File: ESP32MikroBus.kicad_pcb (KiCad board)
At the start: 4 copper layers, 30.2 x 44.5 mm, 27 parts, among them IC1 ESP32-C6-WROOM-1-N4, IC2 AP7361C-33ER-13, J1 USB4105GFA120, J2 CON_HDR_MIKROBUS_SOCKET_TH, J3 Qwiic, U1 USBLC6-2P6

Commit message: PCB Layout v1.0 ready for verification by PCBWay
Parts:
- added G***: OpenSourceHardware_Logo, tecnova:OpenSourceHardware_Logo, B.Cu at (35.8, 43.3)
- added G***: LOGO, tecnova:Tecnova_logo, B.Cu at (54.7, 42.8)
- added G***: MikroBus_Logo, tecnova:MikroBus_Logo, B.Cu at (43.8, 63.2)
- added J4: Conn_01x06, Connector_PinHeader_1.27mm:PinHeader_1x06_P1.27mm_Vertical, F.Cu at (57.2, 47.4)
- moved R4 15.1 mm to (51.2, 68.7)
- moved R2 14.8 mm to (51.2, 71.8), turned to -90 degrees
- moved TP1 12.7 mm to (50.5, 46.2)
- moved FID2 9.62 mm to (58.5, 39.0)
- moved FID3 8.83 mm to (36.6, 60.4)
- moved FID1 6.46 mm to (30.1, 80.8)
- moved C5 4.89 mm to (50.0, 64.6), turned to 90 degrees
- moved R5 4.80 mm to (41.0, 70.1)
- moved U1 3.65 mm to (43.5, 70.0), turned to 90 degrees
- moved C4 3.32 mm to (50.0, 60.5), turned to -90 degrees
- moved R6 2.21 mm to (46.0, 70.0)
- moved F1 1.75 mm to (48.2, 69.2), turned to -90 degrees
- moved R3 1.00 mm to (56.2, 56.7)
- moved R8 0.53 mm to (56.5, 44.2)
- moved J2 0.12 mm to (44.2, 69.3)
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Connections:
- C5 pad 1: Net-(IC2-IN) -> +5V
- F1 pad 1: +VBUS -> +5V
- F1 pad 2: +5V -> +VBUS
- IC1 pad 10: unconnected-(IC1-IO8-Pad10) -> /MB_MISO
- IC1 pad 11: unconnected-(IC1-IO10-Pad11) -> /MB_SCK
- IC1 pad 12: unconnected-(IC1-IO11-Pad12) -> /MB_CS
- IC1 pad 16: unconnected-(IC1-IO18-Pad16) -> /SPARE6
- IC1 pad 17: unconnected-(IC1-IO19-Pad17) -> /SPARE5
- IC1 pad 18: unconnected-(IC1-IO20-Pad18) -> /SPARE4
- IC1 pad 19: unconnected-(IC1-IO21-Pad19) -> /SPARE3
- IC1 pad 20: unconnected-(IC1-IO22-Pad20) -> /SPARE2
- IC1 pad 21: unconnected-(IC1-IO23-Pad21) -> /SPARE1
- IC1 pad 26: unconnected-(IC1-IO3-Pad26) -> /MB_PWM
- IC1 pad 27: unconnected-(IC1-IO2-Pad27) -> /USR_LED
- IC1 pad 4: unconnected-(IC1-IO4-Pad4) -> /MB_INT
- IC1 pad 5: unconnected-(IC1-IO5-Pad5) -> /MB_RST
- IC1 pad 9: unconnected-(IC1-IO1-Pad9) -> /MB_MOSI
- IC2 pad 3: Net-(IC2-IN) -> +5V
- J2 pad 15: Net-(J2-+5V) -> +5V
- R3 pad 1: +3V3 -> +3.3V
- R7 pad 1: Net-(R7-Pad1) -> +5V
- S1 pad 4: Net-(S1-Pad4) -> GND
- S1 pad 6: Net-(S1-Pad4) -> GND
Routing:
- net GND: track 0.00 -> 78.3 mm, vias 0 -> 12
- net +3.3V: track 0.00 -> 61.1 mm, vias 0 -> 9
- net /I2C_SDA: track 0.00 -> 55.7 mm, vias 0 -> 2
- net /I2C_SCL: track 0.00 -> 47.9 mm, vias 0 -> 2
- net /TXD: track 0.00 -> 35.6 mm
- net /RXD: track 0.00 -> 32.3 mm
- net /MB_INT: track 0.00 -> 31.5 mm, vias 0 -> 1
- net /MB_MOSI: track 0.00 -> 29.1 mm
- net /MB_RST: track 0.00 -> 27.4 mm, vias 0 -> 1
- net /MB_PWM: track 0.00 -> 26.2 mm, vias 0 -> 1
- net /MB_MISO: track 0.00 -> 25.1 mm
- net /MB_SCK: track 0.00 -> 21.2 mm
- net +5V: track 0.00 -> 19.4 mm
- net /USB_D_MIN: track 0.00 -> 18.7 mm, vias 0 -> 2
- net /USB_D_PLUS: track 0.00 -> 18.7 mm, vias 0 -> 2
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- added copper zone on In2.Cu, net +3.3V
- added copper zone on In2.Cu, net +VBUS
- added copper zone on In1.Cu, net GND
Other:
- board size 30.2 x 44.5 mm -> 31 x 44.8 mm
- board text added: "ESP32C6 + mikroBUS v1.0"
- board text added: "Reset"

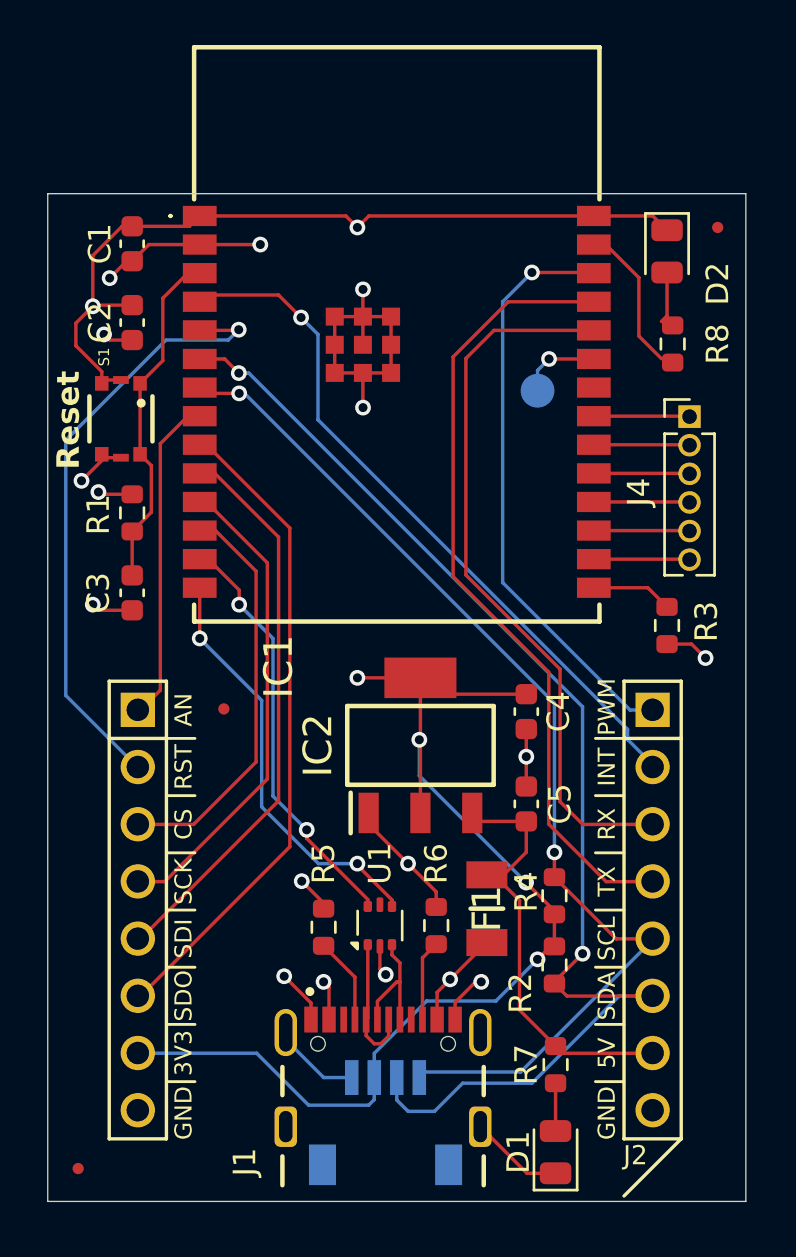
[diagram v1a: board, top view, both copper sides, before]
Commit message: Minor update, mainly cosmetical + vbus not connected
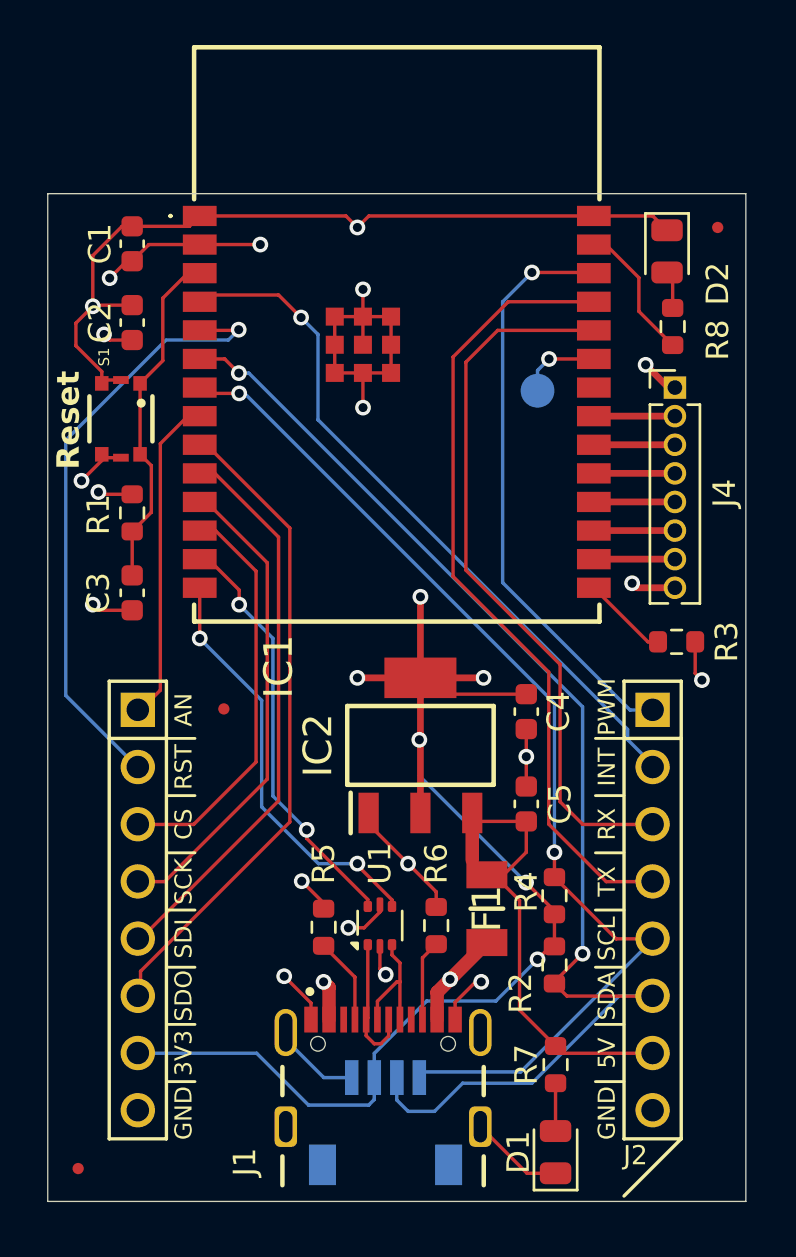
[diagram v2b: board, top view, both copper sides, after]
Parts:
- J4: value Conn_01x06 -> Conn_01x08; footprint Connector_PinHeader_1.27mm:PinHeader_1x06_P1.27mm_Vertical -> Connector_PinHeader_1.27mm:PinHeader_1x08_P1.27mm_Vertical
- moved J4 1.44 mm to (56.6, 46.1)
- moved R3 0.84 mm to (56.7, 57.4), turned to 180 degrees
- moved R8 0.77 mm to (56.5, 43.4)
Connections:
- J4 pad 1: /SPARE1 -> +3.3V
- J4 pad 2: /SPARE2 -> /SPARE1
- J4 pad 3: /SPARE3 -> /SPARE2
- J4 pad 4: /SPARE4 -> /SPARE3
- J4 pad 5: /SPARE5 -> /SPARE4
- J4 pad 6: /SPARE6 -> /SPARE5
- U1 pad 5: Net-(U1-VBUS) -> +VBUS
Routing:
- net +3.3V: track 61.1 -> 69.1 mm, vias 9 -> 12
- net +5V: track 19.4 -> 22.4 mm
- net +VBUS: track 6.11 -> 8.12 mm, vias 2 -> 3
- net GND: track 78.3 -> 80.2 mm, vias 12 -> 13
- net /SPARE6: track 4.26 -> 3.60 mm
- net /SPARE4: track 4.26 -> 3.60 mm
- net /SPARE2: track 4.26 -> 3.60 mm
- net /SPARE5: track 4.26 -> 3.60 mm
- net /SPARE3: track 4.26 -> 3.60 mm
- net /SPARE1: track 4.26 -> 3.63 mm
- net Net-(D2-A): track 2.28 -> 1.68 mm

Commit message: Changed c1 to 10uF, more attention to power traces, fixed copper plane and qwiic connector
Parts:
- moved FID3 9.59 mm to (37.8, 69.9)
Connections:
- J3 pad 1: /I2C_SCL -> GND
- J3 pad 2: /I2C_SDA -> +3.3V
- J3 pad 3: +3.3V -> /I2C_SDA
- J3 pad 4: GND -> /I2C_SCL
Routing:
- net +3.3V: track 69.1 -> 61.3 mm, vias 12 -> 11
- net /I2C_SDA: track 55.7 -> 60.2 mm
- net /I2C_SCL: track 47.9 -> 49.9 mm
- net GND: track 80.2 -> 79.9 mm, vias 13 -> 14
